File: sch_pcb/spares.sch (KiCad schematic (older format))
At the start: 85 parts, among them J301 SPARE, J302 SPARE, J303 SPARE, J304 SPARE, J305 AUX_IO_1, J306 SPARE, J307 SPARE, J308 AUX_IO_2, J309 SPARE, J310 SPARE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

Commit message: Add files via upload
Fix sheet ordering in schematic
Finish routing (except USB connector...)
Still to do: USB connector, cleanup PCB, fix refdes positions
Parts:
- added LOGO301: MOUNTING_HOLE, lib:BOBCAT_LOGO, symbol MOUNTING_HOLE
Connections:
- no-connect marks 7 -> 8
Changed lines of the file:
@@
 Text Label 8425 1600 0    60   ~ 0
 SCL0_OUT
+$Comp
+L MOUNTING_HOLE LOGO301
+U 1 1 598BD8CD
+P 9225 6425
+F 0 "LOGO301" H 9225 6550 60  0000 C CNN
+F 1 "MOUNTING_HOLE" H 9225 6575 60  0001 C CNN
+F 2 "lib:BOBCAT_LOGO" H 9225 6425 60  0001 C CNN
+F 3 "" H 9225 6425 60  0000 C CNN
+	1    9225 6425
+	1    0    0    -1
+$EndComp
+NoConn ~ 9225 6425
 $EndSCHEMATC

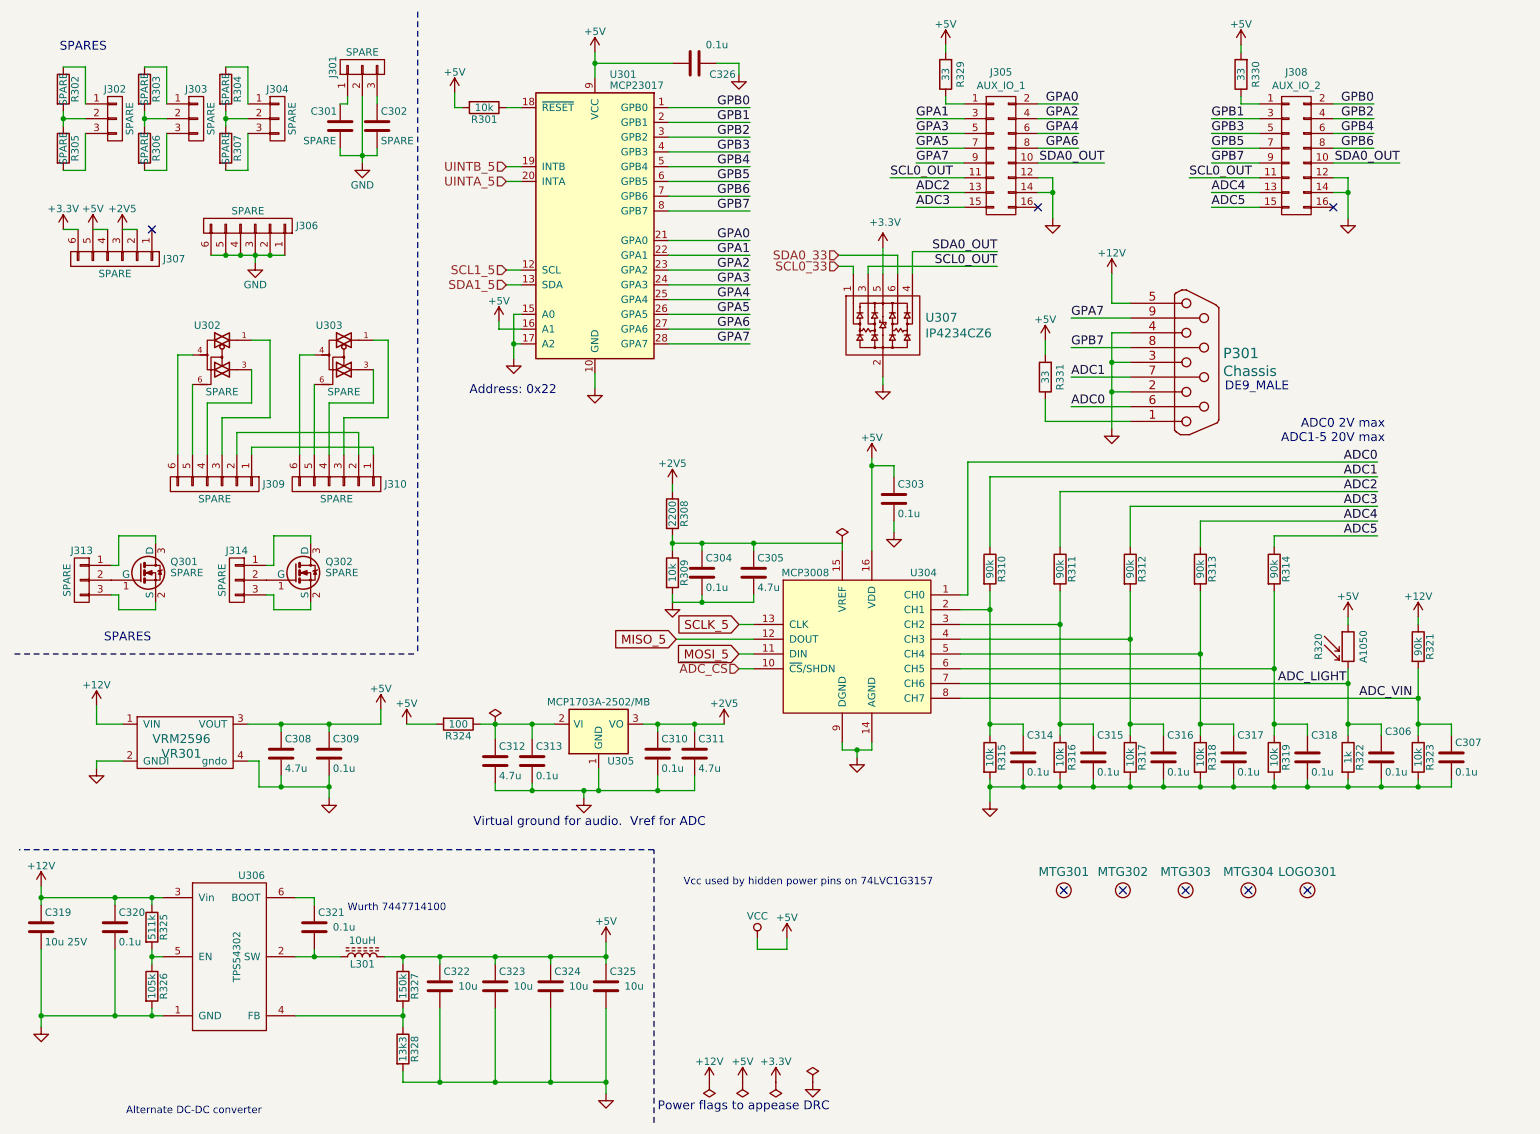
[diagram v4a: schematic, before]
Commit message: Update board with third soundcard
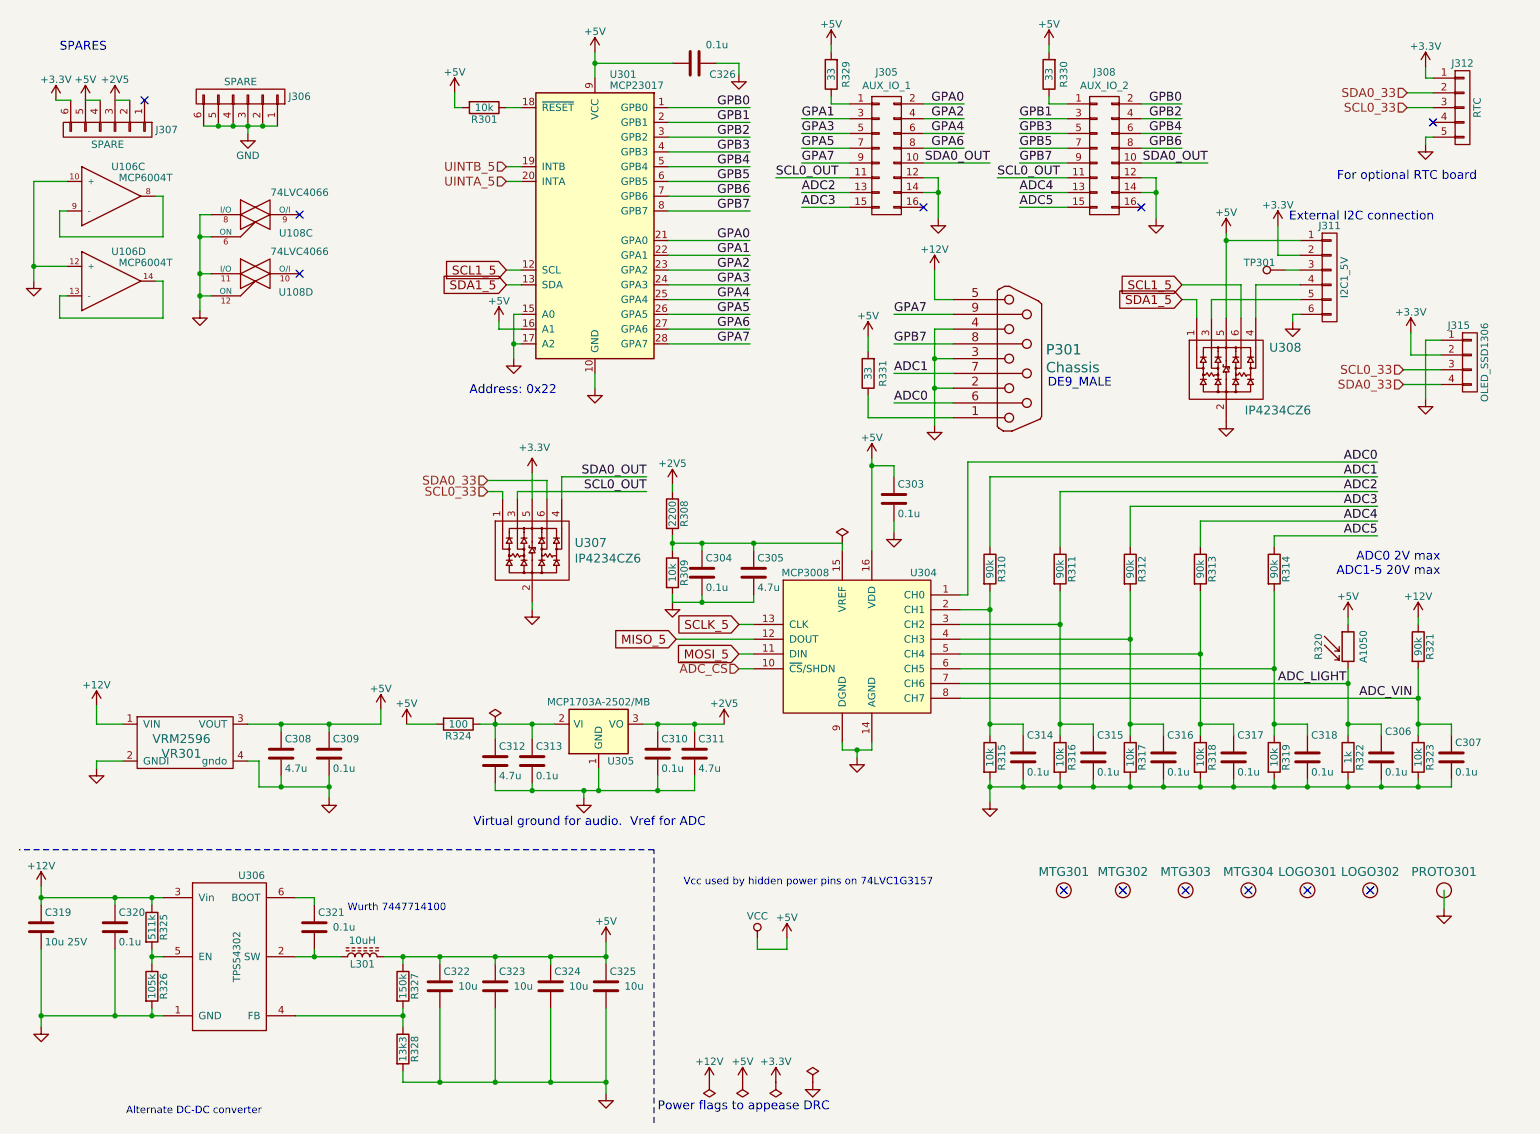
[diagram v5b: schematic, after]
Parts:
- removed C301, C302: SPARE, lib:smd0603, symbol C
- removed J301, J302, J303, J304, J313, J314: SPARE, lib:SIL-3, symbol CONN_01X03
- removed J309, J310: SPARE, lib:SIL-6, symbol CONN_01X06
- removed Q301, Q302: SPARE, lib:SOT23, symbol 2N7002
- removed R302, R303, R304, R305, R306, R307: SPARE, lib:smd0603, symbol R
- removed U302, U303: SPARE, lib:SOT23-6, symbol 74LVC1G3157
- added J311: I2C1_5V, lib:SIL-6, symbol CONN_01X06
- added J312: RTC, lib:SIL-5, symbol CONN_01X05
- added J315: OLED_SSD1306, lib:SIL-4, symbol CONN_01X04
- added LOGO302: MOUNTING_HOLE, lib:mmra_logo, symbol MOUNTING_HOLE
- added PROTO301: MOUNTING_HOLE, lib:SMD_proto_area, symbol MOUNTING_HOLE
- added TP301: TESTPOINT, lib:Wire_28AWG, symbol TESTPOINT
- added U106: MCP6004T, lib:SOIC14, symbol MCP6004N
- added U108: 74LVC4066, lib:SOIC14, symbol 74LVC4066
- added U308: IP4234CZ6, lib:SOT23-6, symbol IP4234CZ6_USB_ESD_PROTECTOR
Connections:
- net +3V3: now also J311.2 (P2), J312.1 (P1), J315.2 (P2)
- net +5V: now also J311.1 (P1), U308.5
- net GND: now also J311.6 (P6), J312.5 (P5), J315.1 (P1), PROTO301.1, U106.10 (+), U106.12 (+), U108.11 (I/O), U108.12 (ON), U108.6 (ON), U108.8 (I/O), U308.2
- net SCL0_33: now also J312.3 (P3), J315.3 (P3)
- net SCL1_5: now also U308.6
- net SDA0_33: now also J312.2 (P2), J315.4 (P4)
- net SDA1_5: now also U308.1
- new net: J311.3 (P3), TP301.1
- new net: J311.4 (P4), U308.4
- new net: J311.5 (P5), U308.3
- new net: U106.8 (OUT), U106.9 (-)
- new net: U106.13 (-), U106.14 (OUT)
- no-connect marks 8 -> 12
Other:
- note added: "External I2C connection"
- note added: "For optional RTC board"
- moved on the sheet: J305, J306, J307, J308, P301, R329, R330, R331, U307

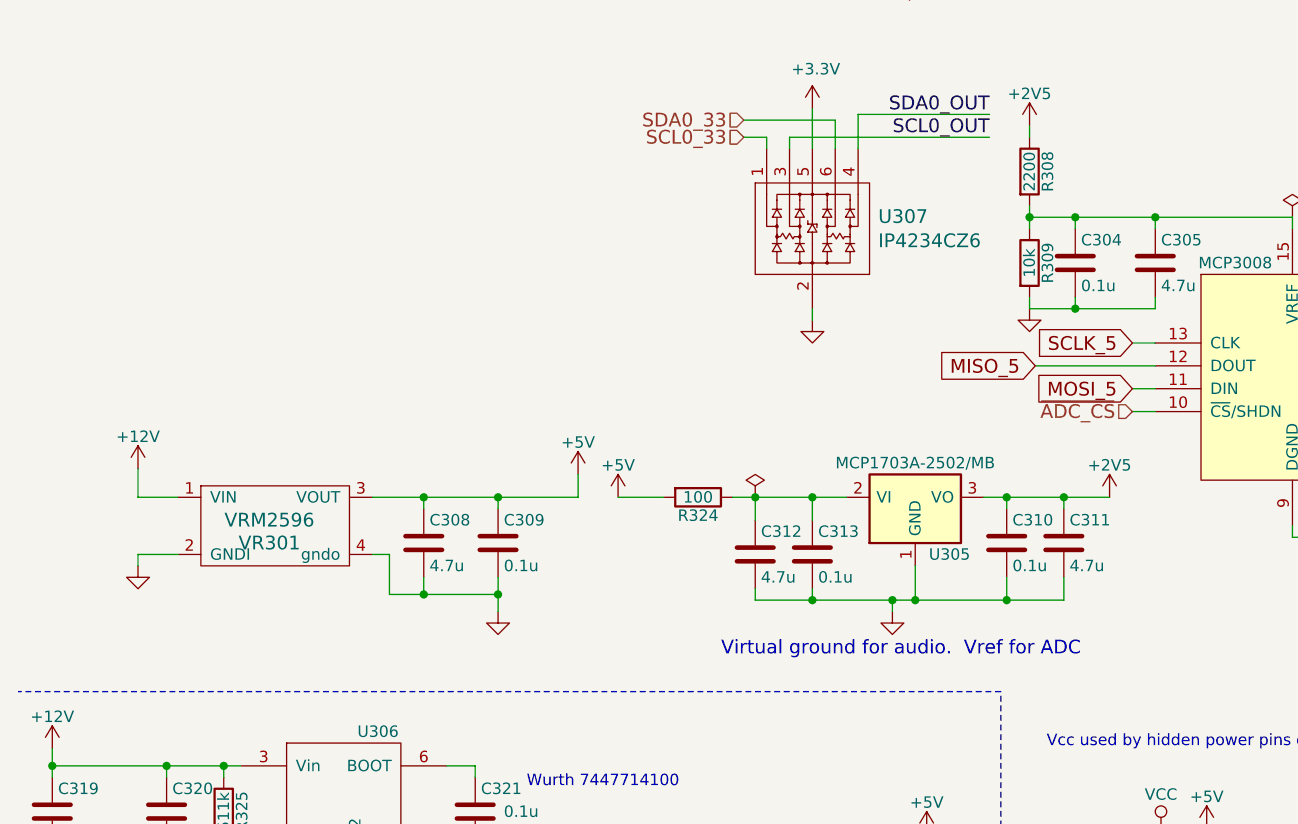
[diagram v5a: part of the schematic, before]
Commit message: Add minimum load on 2v5 regulator.  Update gain to soundcard 1 and 2
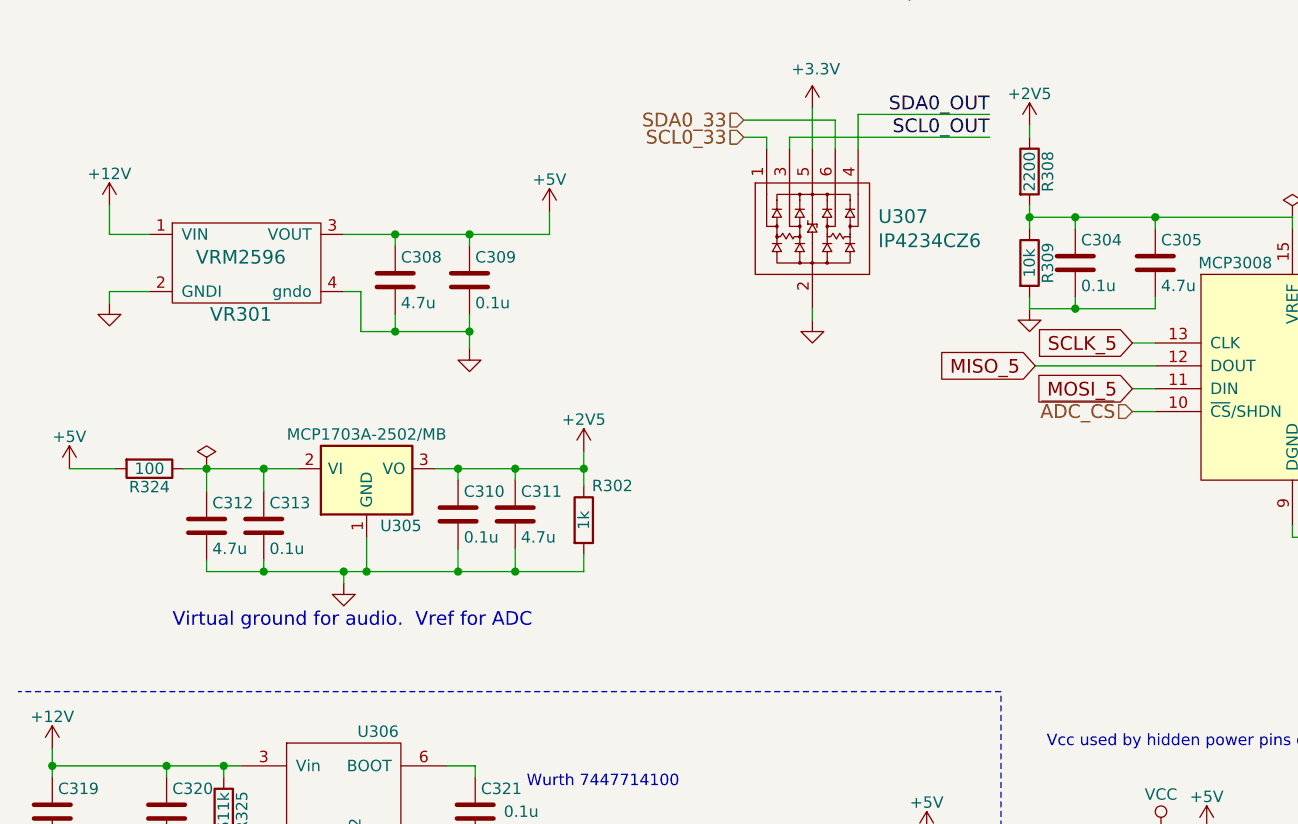
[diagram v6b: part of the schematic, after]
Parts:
- added R302: 1k, lib:smd0603, symbol R
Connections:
- net +2V5: now also R302.1
- net GND: now also R302.2
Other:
- moved on the sheet: C308, C309, C310, C311, C312, C313, R324, U305, VR301

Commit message: BOM scrub
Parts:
- R325: value 511k -> SPARE
- R326: value 105k -> SPARE
- R327: value 150k -> 100k
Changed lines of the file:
@@
 U 1 1 5963A47D
 P 1150 6675
-F 0 "C320" H 1175 6775 50  0000 L CNN
+F 0 "C320" H 950 6775 50  0000 L CNN
 F 1 "0.1u" H 1175 6575 50  0000 L CNN
 F 2 "lib:smd0603" H 1188 6525 50  0001 C CNN
@@
 P 3100 7075
 F 0 "R327" V 3180 7075 50  0000 C CNN
-F 1 "150k" V 3100 7075 50  0000 C CNN
+F 1 "100k" V 3100 7075 50  0000 C CNN
 F 2 "lib:smd0603" V 3030 7075 50  0001 C CNN
 F 3 "" H 3100 7075 50  0001 C CNN
@@
 P 1400 6675
 F 0 "R325" V 1480 6675 50  0000 C CNN
-F 1 "511k" V 1400 6675 50  0000 C CNN
+F 1 "SPARE" V 1550 6675 50  0000 C CNN
 F 2 "lib:smd0603" V 1330 6675 50  0001 C CNN
 F 3 "" H 1400 6675 50  0001 C CNN
@@
 P 1400 7075
 F 0 "R326" V 1480 7075 50  0000 C CNN
-F 1 "105k" V 1400 7075 50  0000 C CNN
+F 1 "SPARE" V 1550 7075 50  0000 C CNN
 F 2 "lib:smd0603" V 1330 7075 50  0001 C CNN
 F 3 "" H 1400 7075 50  0001 C CNN

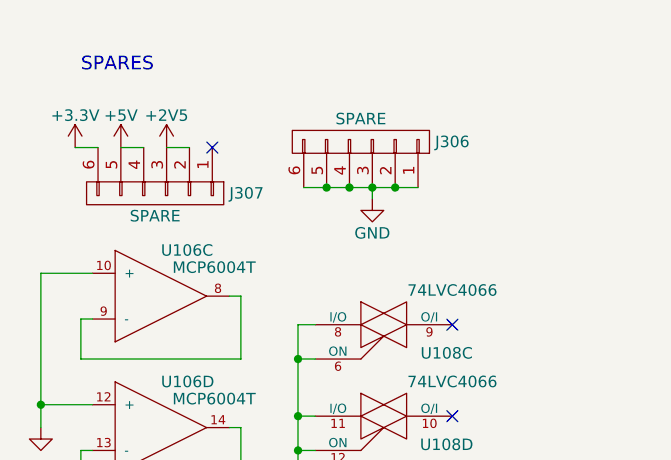
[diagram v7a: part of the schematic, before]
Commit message: Move link connector close to edge to allow using jumpers to connect boards
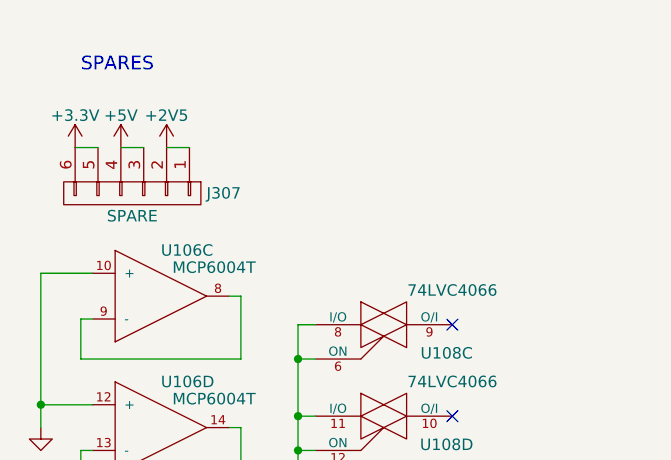
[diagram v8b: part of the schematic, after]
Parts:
- removed J306: SPARE, lib:SIL-6, symbol CONN_01X06
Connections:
- net +2V5: now also J307.1 (P1); no longer J307.3 (P3)
- net +3V3: now also J307.5 (P5)
- net +5V: now also J307.3 (P3); no longer J307.5 (P5)
- no-connect marks 12 -> 11
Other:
- moved on the sheet: J307
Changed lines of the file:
@@
-$EndComp
-$Comp
-L GND #PWR0308
-U 1 1 5967F201
-P 2050 1300
-F 0 "#PWR0308" H 2050 1050 50  0001 C CNN
-F 1 "GND" H 2050 1150 50  0000 C CNN
-F 2 "" H 2050 1300 50  0001 C CNN
-F 3 "" H 2050 1300 50  0001 C CNN
-	1    2050 1300
-	1    0    0    -1
 $EndComp
 $Comp
@@
 L CONN_01X06 J307
 U 1 1 5967F264
-P 1100 1275
-F 0 "J307" V 1100 1675 50  0000 C CNN
-F 1 "SPARE" V 1200 1275 50  0000 C CNN
-F 2 "lib:SIL-6" H 1100 1275 50  0001 C CNN
-F 3 "" H 1100 1275 50  0001 C CNN
-	1    1100 1275
+P 1000 1275
+F 0 "J307" V 1000 1675 50  0000 C CNN
+F 1 "SPARE" V 1100 1275 50  0000 C CNN
+F 2 "lib:SIL-6" H 1000 1275 50  0001 C CNN
+F 3 "" H 1000 1275 50  0001 C CNN
+	1    1000 1275
 	0    1    1    0
-$EndComp
-$Comp
-L CONN_01X06 J306
-U 1 1 5967F26E
-P 2000 1050
-F 0 "J306" V 2000 1450 50  0000 C CNN
-F 1 "SPARE" V 2100 1050 50  0000 C CNN
-F 2 "lib:SIL-6" H 2000 1050 50  0001 C CNN
-F 3 "" H 2000 1050 50  0001 C CNN
-	1    2000 1050
-	0    1    -1   0
 $EndComp
 Text Notes 775  750  0    60   ~ 0
@@
 Text GLabel 4950 4725 0    60   Input ~ 0
 MISO_5
-NoConn ~ 1350 1075
 $Comp
 L +5V #PWR0328
@@
 	1250 1075 1150 1075
 Wire Wire Line
-	1750 1250 2250 1250
-Connection ~ 1850 1250
-Connection ~ 1950 1250
-Connection ~ 2050 1250
-Connection ~ 2150 1250
-Wire Wire Line
-	2050 1300 2050 1250
-Wire Wire Line
 	4400 3025 4400 2925
